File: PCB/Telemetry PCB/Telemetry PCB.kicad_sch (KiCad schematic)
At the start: 9 parts, among them U1 STM32F411CEUx, Y1 25MHZ 9pF, Y2 32.768k 6pF

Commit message: Boot, reset and VREF circuits and programming header added
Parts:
- added C10: 1uF, symbol Device:C
- added C11, C12, C6, C7, C8, C9: 0.1uF, symbol Device:C
- added J1: Conn_01x04_Pin, symbol Connector:Conn_01x04_Pin
- added R1, R2, R3: 10K, symbol Device:R
- added SW1, SW2: SW_MEC_5E, symbol Switch:SW_MEC_5E
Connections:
- net +3.3V: now also C6.1, C7.1, C8.1, J1.1 (Pin_1), R1.1, SW2.3 (K), SW2.4 (A)
- net BOOT0: now also C12.2, R2.2, SW2.1, SW2.2
- net GND: now also C10.2, C11.2, C12.1, C6.2, C7.2, C8.2, C9.2, J1.4 (Pin_4), R2.1, R3.1, SW1.3 (K), SW1.4 (A)
- net NRST: now also C11.1, R1.2, SW1.1, SW1.2
- net PB2: now reaches U1.20 (PB2)
- net PB2: now also R3.2
- net SWDIO: now reaches U1.34 (PA13)
- net SWDIO: now also J1.2 (Pin_2)
- net SWCLK: now reaches U1.37 (PA14)
- net SWCLK: now also J1.3 (Pin_3)
- net VREF+: now reaches L1.1, U1.9 (VDDA)
- net VREF+: now also C10.1, C9.1
- net VBAT: no longer names the net of U1.1 (VBAT)
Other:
- note added: "Boot Selection"
- note added: "Debug/Programming Header"
- note added: "Reset Circuit"
- note added: "VREF STABILIZATION"
- moved on the sheet: L1

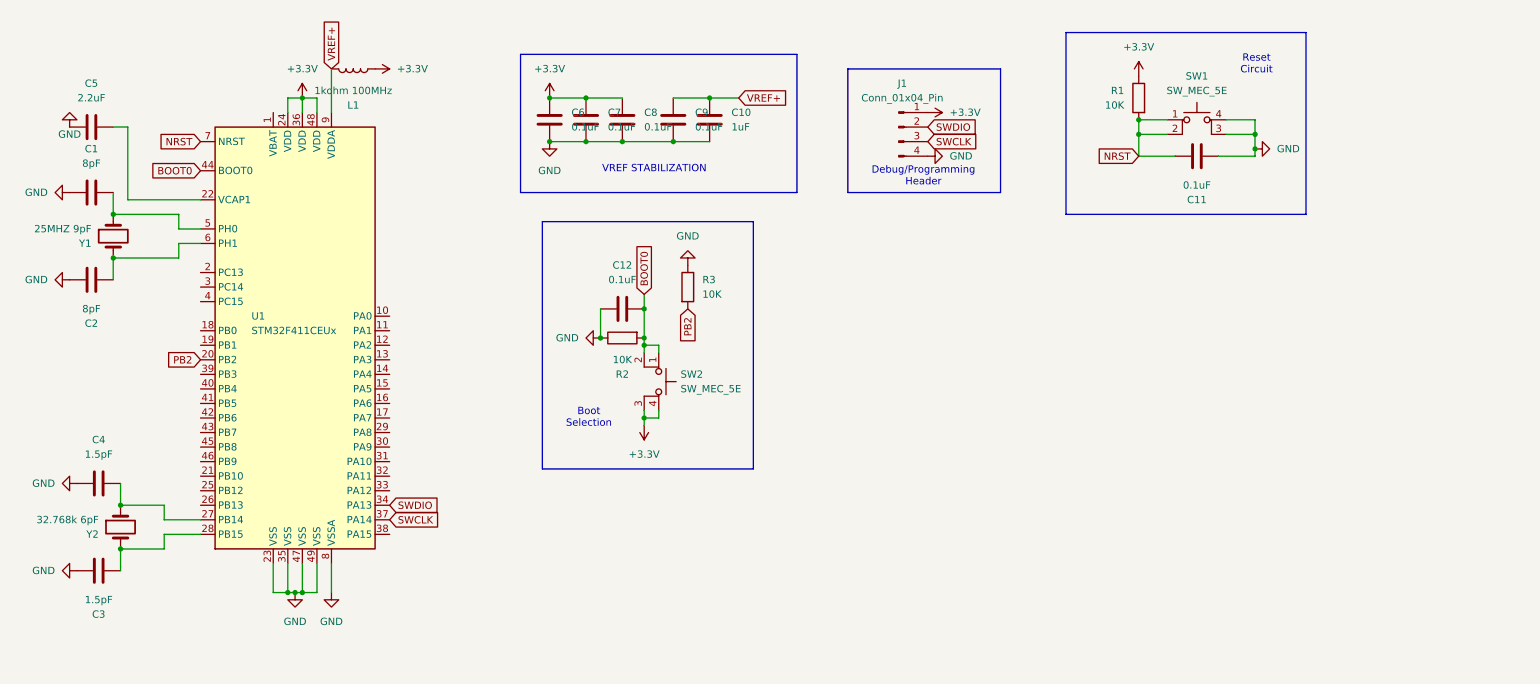
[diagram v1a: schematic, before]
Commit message: E22-900M33s initial circuitry added
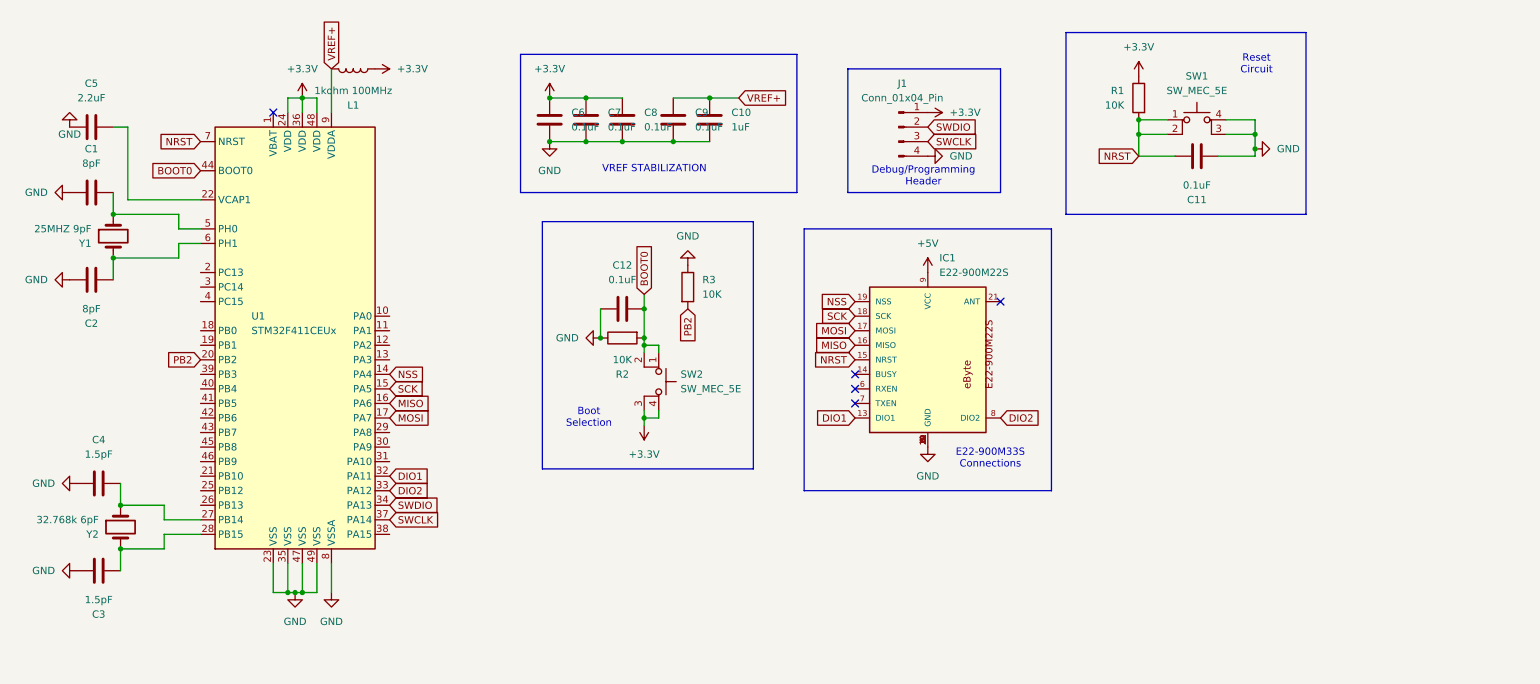
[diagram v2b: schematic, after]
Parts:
- added IC1: E22-900M22S, E22-900M22S:E22-900M22S, symbol E22-900M22S:E22-900M22S
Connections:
- net GND: now also IC1.1 (GND), IC1.10 (GND), IC1.11 (GND), IC1.12 (GND), IC1.2 (GND), IC1.20 (GND), IC1.22 (GND), IC1.3 (GND), IC1.4 (GND), IC1.5 (GND)
- net NRST: now also IC1.15 (NRST)
- net NSS: now reaches U1.14 (PA4)
- net NSS: now also IC1.19 (NSS)
- net SCK: now reaches U1.15 (PA5)
- net SCK: now also IC1.18 (SCK)
- net MISO: now reaches U1.16 (PA6)
- net MISO: now also IC1.16 (MISO)
- net MOSI: now reaches U1.17 (PA7)
- net MOSI: now also IC1.17 (MOSI)
- net DIO1: now reaches U1.32 (PA11)
- net DIO1: now also IC1.13 (DIO1)
- net DIO2: now reaches U1.33 (PA12)
- net DIO2: now also IC1.8 (DIO2)
- new net +5V: IC1.9 (VCC)
- no-connect marks 0 -> 5
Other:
- note added: "E22-900M33S Connections"

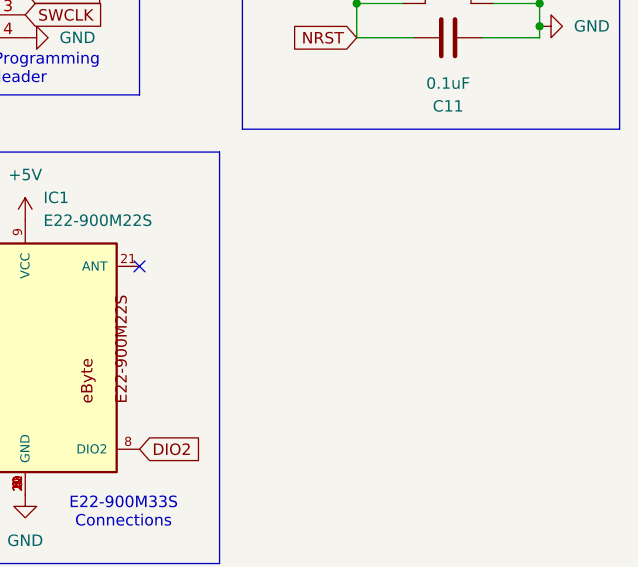
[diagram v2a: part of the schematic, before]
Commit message: Added gps connection
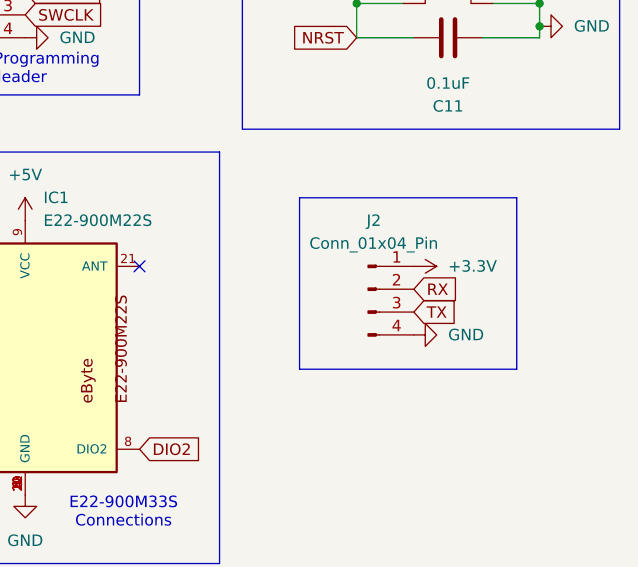
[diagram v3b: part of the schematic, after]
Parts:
- added J2: Conn_01x04_Pin, symbol Connector:Conn_01x04_Pin
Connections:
- net +3.3V: now also J2.1 (Pin_1)
- net GND: now also J2.4 (Pin_4)
- new net RX: J2.2 (Pin_2)
- new net TX: J2.3 (Pin_3)

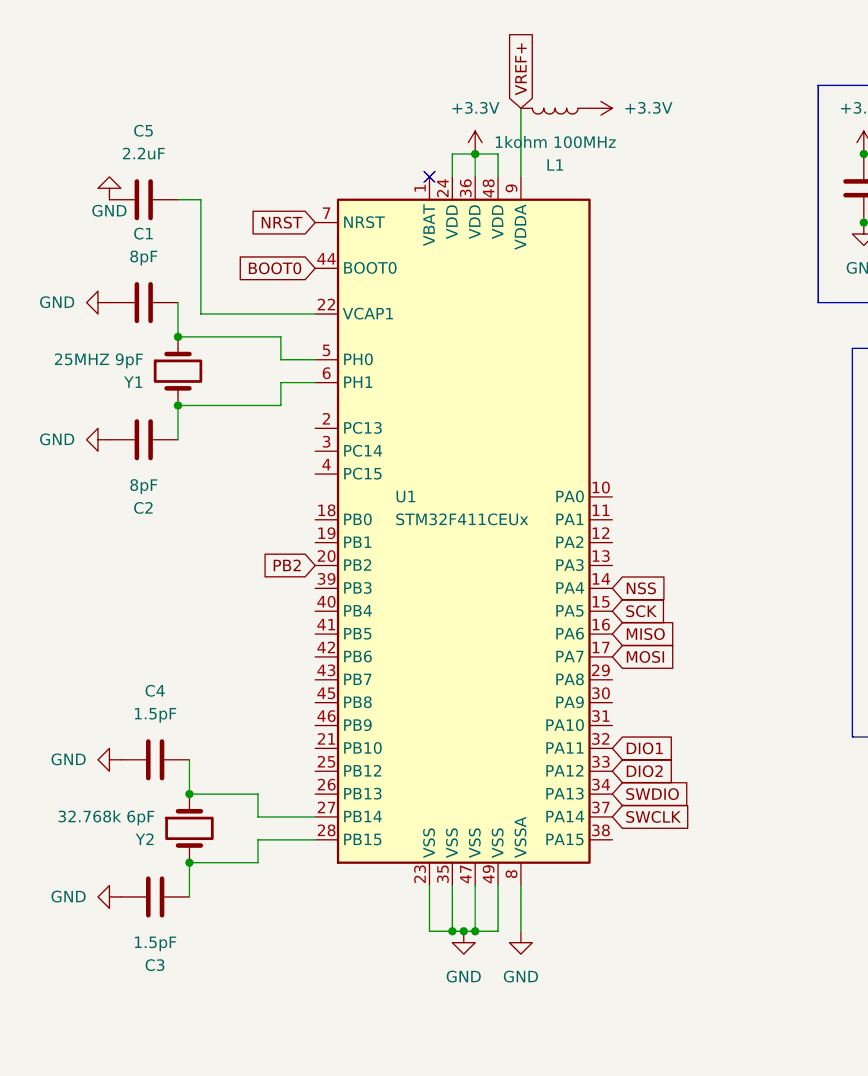
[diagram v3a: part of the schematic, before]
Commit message: Update e22-900m33s library and add gps connection to mcu
e22-900m33s had wrong footprint library. Library has been updated to proper one.
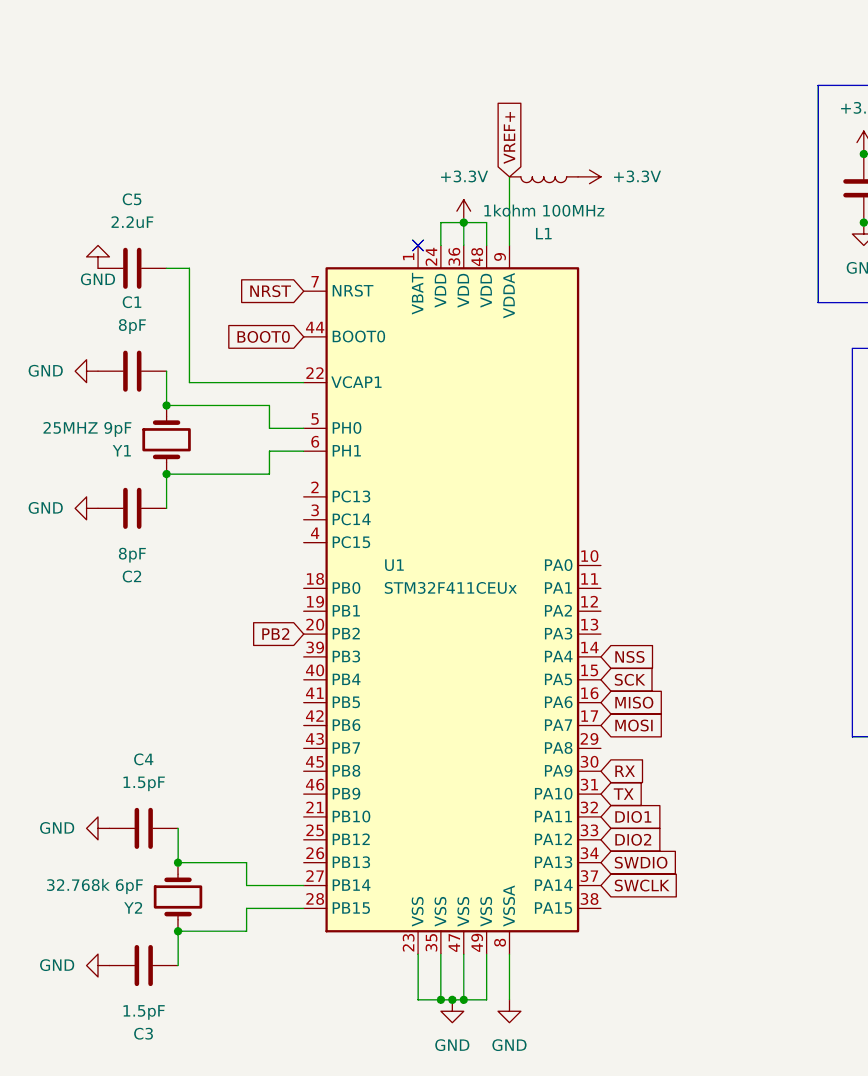
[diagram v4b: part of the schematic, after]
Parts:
- IC1: footprint E22-900M22S:E22-900M22S -> E22-900M30S:XCVR_E22-900M30S
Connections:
- net RX: now also U1.30 (PA9)
- net TX: now also U1.31 (PA10)
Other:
- moved on the sheet: C1, C2, C3, C4, C5, L1, U1, Y1, Y2

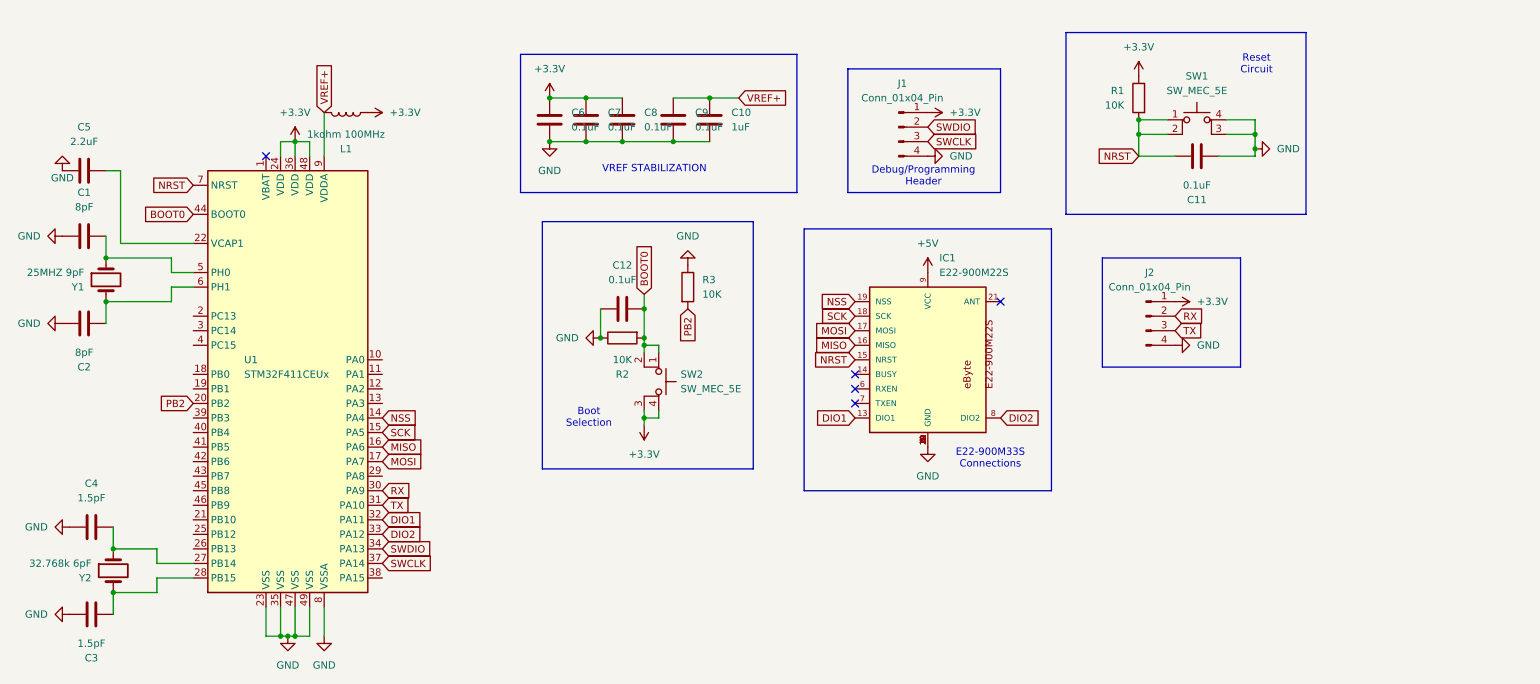
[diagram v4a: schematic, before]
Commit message: Added buck converter circuit
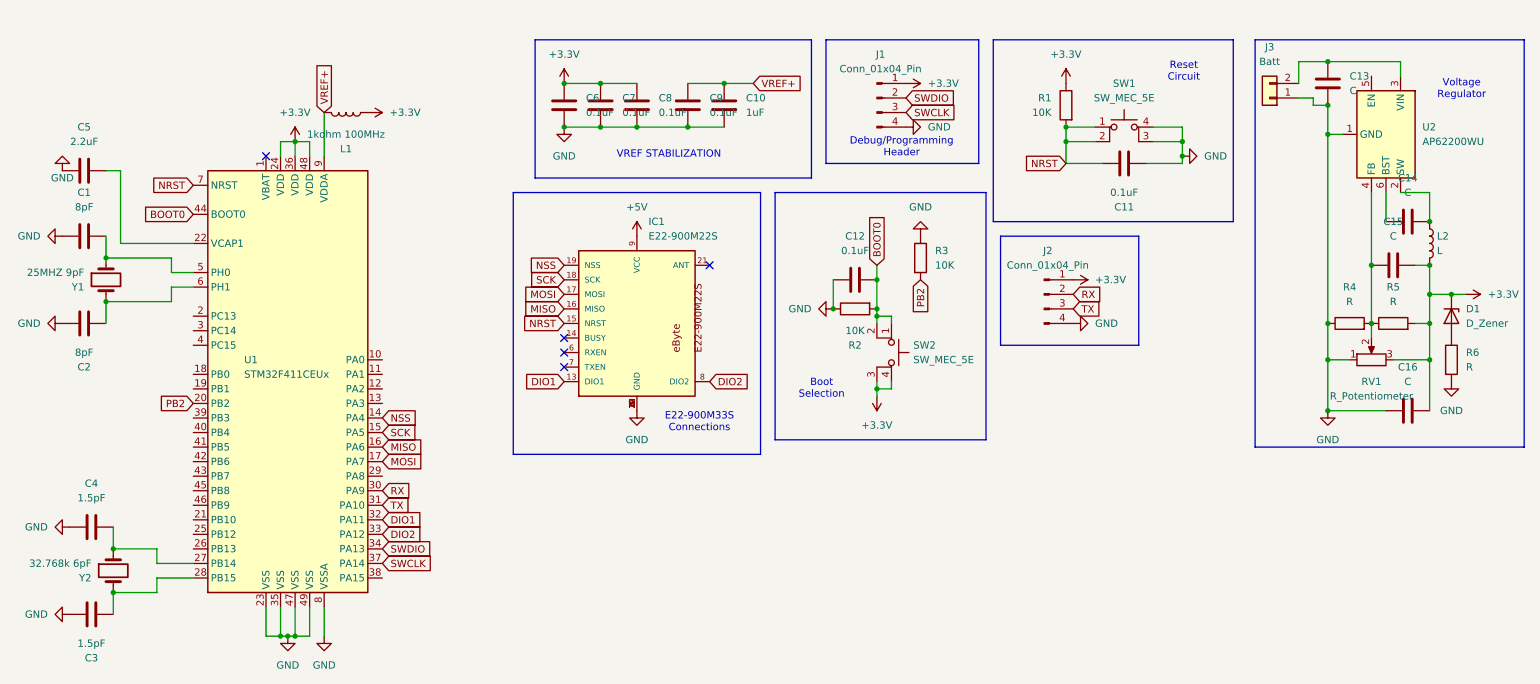
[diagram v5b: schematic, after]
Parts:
- added C13, C14, C15, C16: C, symbol Device:C
- added D1: D_Zener, symbol Device:D_Zener
- added J3: Batt, symbol Connector_Generic:Conn_01x02
- added L2: L, symbol Device:L
- added R4, R5, R6: R, symbol Device:R
- added RV1: R_Potentiometer, symbol Device:R_Potentiometer
- added U2: AP62200WU, Package_TO_SOT_SMD:TSOT-23-6, symbol Regulator_Switching:AP62250WU
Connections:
- net +3.3V: now also C15.2, C16.2, D1.1 (K), L2.2, R5.2, RV1.3
- net GND: now also C13.2, C16.1, J3.1 (Pin_1), R4.1, R6.2, RV1.1, U2.1 (GND)
- new net: C13.1, J3.2 (Pin_2), U2.3 (VIN)
- new net: C15.1, R4.2, R5.1, RV1.2, U2.4 (FB)
- new net: C14.2, L2.1, U2.2 (SW)
- new net: D1.2 (A), R6.1
- new net: C14.1, U2.6 (BST)
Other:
- note added: "Voltage Regulator"
- moved on the sheet: C10, C11, C12, C6, C7, C8, C9, IC1, J1, J2, R1, R2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

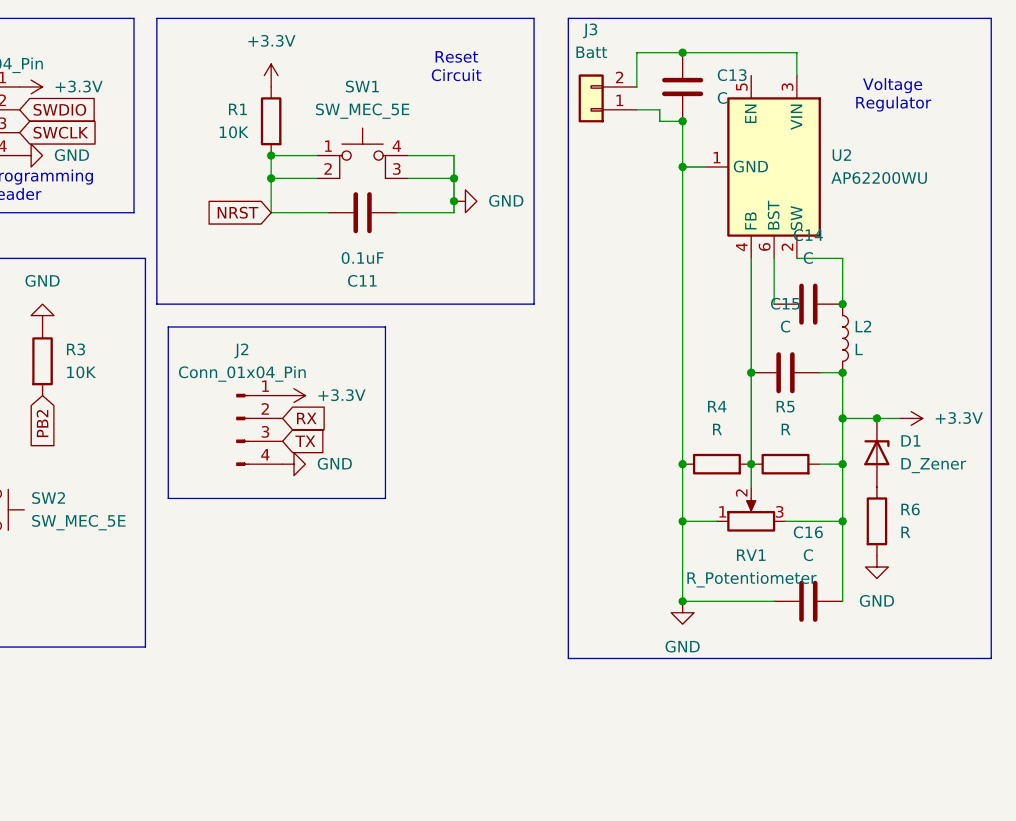
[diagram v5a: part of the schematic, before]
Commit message: Rewired vreg circuit
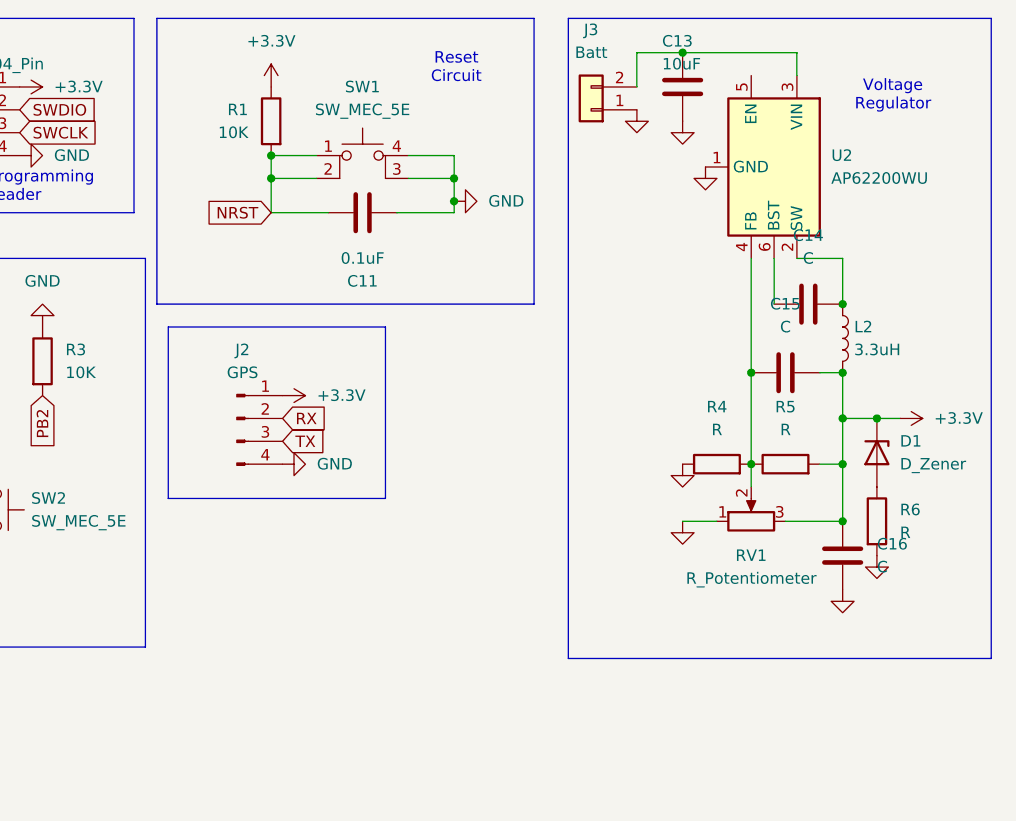
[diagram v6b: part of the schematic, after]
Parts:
- C13: value C -> 10uF
- J2: value Conn_01x04_Pin -> GPS
- L2: value L -> 3.3uH
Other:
- moved on the sheet: C16
